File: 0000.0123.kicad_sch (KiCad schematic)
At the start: 56 parts, among them J1 Conn_02x08_Odd_Even, J6 Conn_01x08, U1 TPA3255

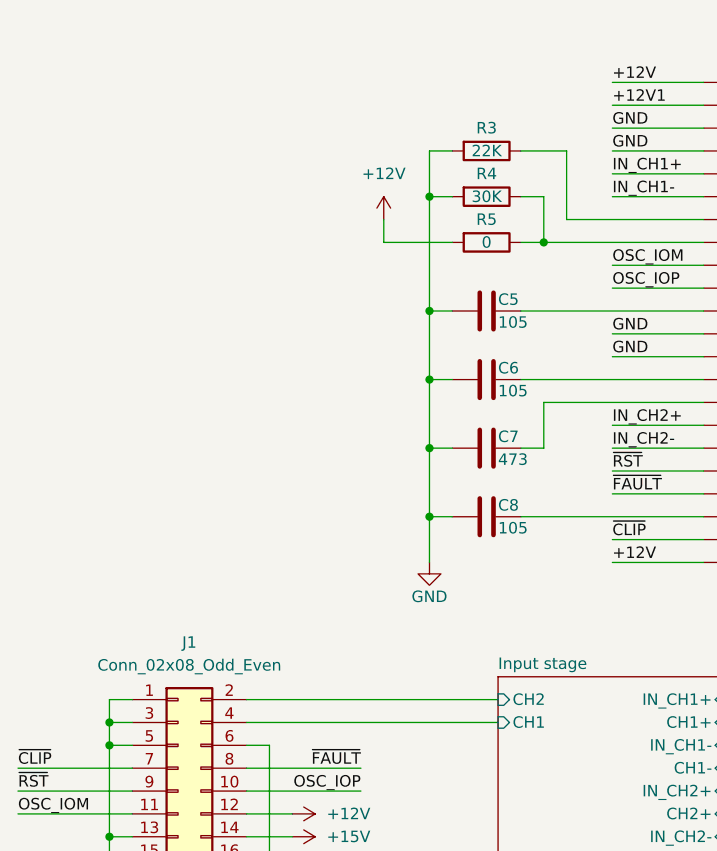
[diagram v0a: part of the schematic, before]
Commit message: Fixed minor error - R5 is now connected to +12V1 instead of +12V.
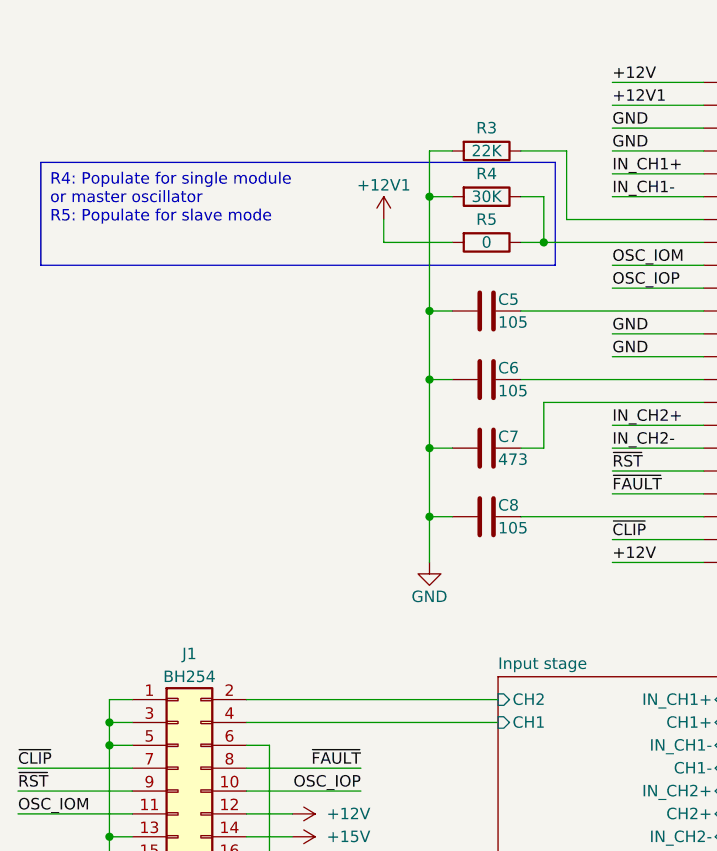
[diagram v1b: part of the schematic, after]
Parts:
- J1: value Conn_02x08_Odd_Even -> BH254
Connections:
- net +12V: no longer R5.2
- net +12V1: now also R5.2
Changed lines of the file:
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@@
 		)
 	)
+	(text_box "R4: Populate for single module\nor master oscillator\nR5: Populate for slave mode"
+		(exclude_from_sim no)
+		(at 27.94 59.69 0)
+		(size 57.15 11.43)
+		(stroke
+			(width 0)
+			(type default)
+		)
+		(fill
+			(type none)
+		)
+		(effects
+			(font
+				(size 1.27 1.27)
+			)
+			(justify left top)
+		)
+	)
 	(label "GND"
 		(at 144.78 99.06 180)
@@
 		(on_board yes)
 		(dnp no)
-		(fields_autoplaced yes)
 		(property "Reference" "J1"
-			(at 44.45 113.03 0)
+			(at 44.45 114.3 0)
 			(effects
 				(font
@@
 			)
 		)
-		(property "Value" "Conn_02x08_Odd_Even"
-			(at 44.45 115.57 0)
+		(property "Value" "BH254"
+			(at 44.45 116.84 0)
 			(effects
 				(font
@@
 		(on_board yes)
 		(dnp no)
-		(fields_autoplaced yes)
 		(property "Reference" "#PWR0101"
 			(at 66.04 69.85 0)
@@
 			)
 		)
-		(property "Value" "+12V"
-			(at 66.04 60.96 0)
+		(property "Value" "+12V1"
+			(at 66.04 62.23 0)
 			(effects
 				(font
@@
 		)
 		(instances
-			(project "3255-2BTL"
+			(project "0000.0123"
 				(path "/9538e4ed-27e6-4c37-b989-9859dc0d49e8"
 					(page "2")
